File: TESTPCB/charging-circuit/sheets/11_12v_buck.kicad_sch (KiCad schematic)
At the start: 15 parts, among them P8 1.27mm/1*3p, U19 TPS54302DDCR_C311983

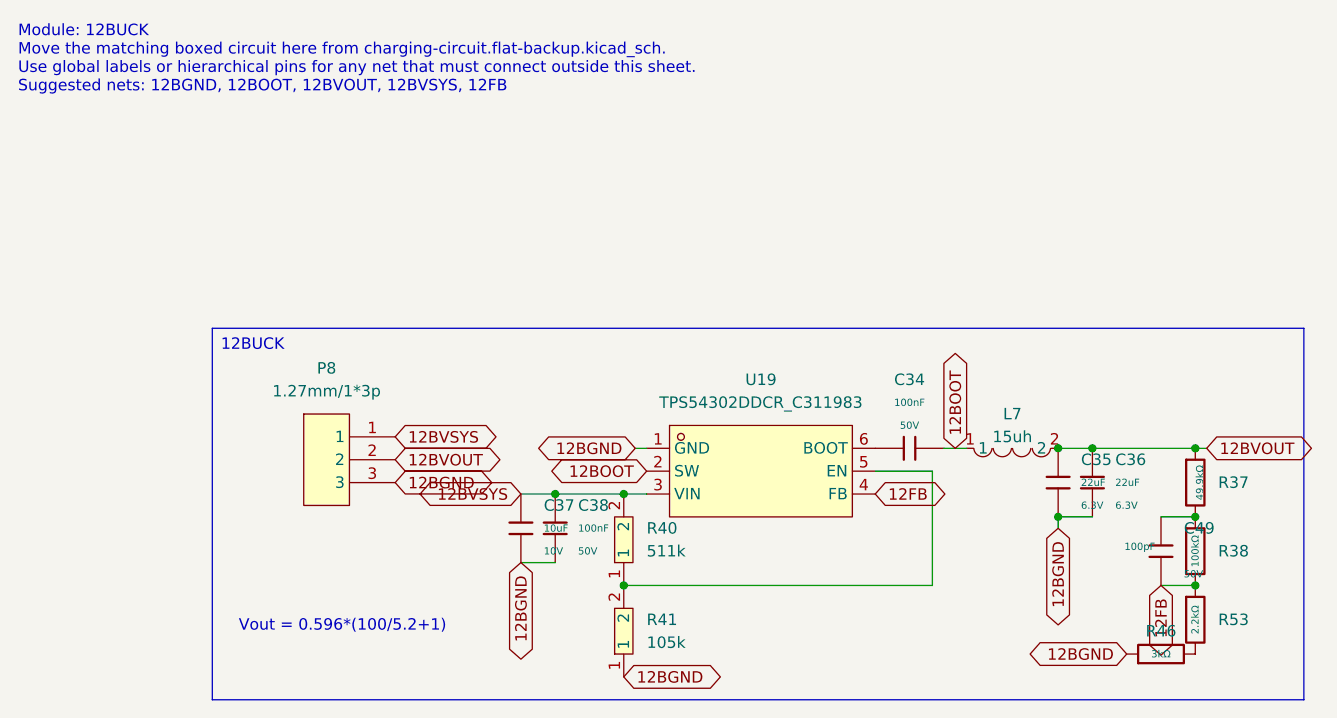
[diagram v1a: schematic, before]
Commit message: Fixed formatting issues, now the hierachal sheets are all labeled as net labels and when we want to expose their pins we will make them into hierchal or global pins
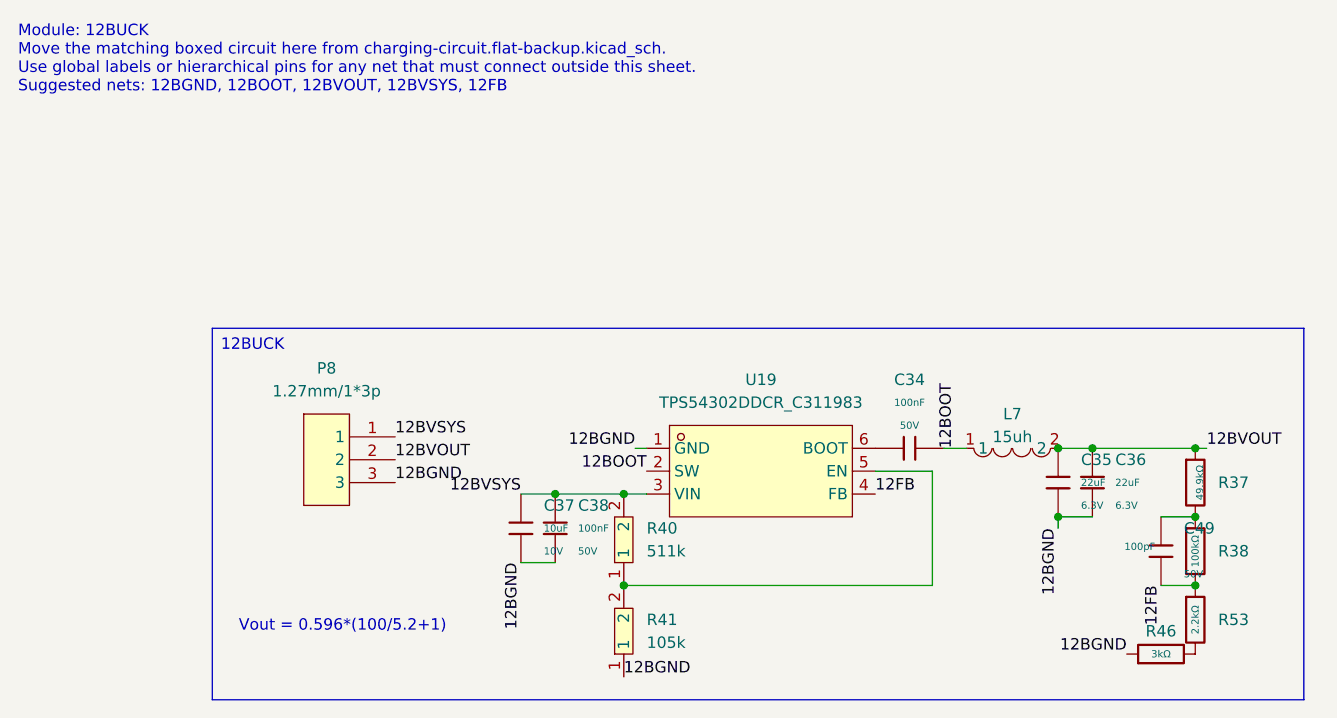
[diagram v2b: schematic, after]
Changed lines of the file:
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@@
 		)
 	)
-	(global_label "12FB"
-		(shape bidirectional)
+	(label "12FB"
 		(at 120.65 73.66 0)
 		(effects
@@
 			(justify left bottom)
 		)
-		(property "Intersheetrefs" "${INTERSHEET_REFS}"
-			(at 120.65 73.66 0)
-			(effects
-				(font
-					(size 1.27 1.27)
-				)
-				(hide yes)
-			)
-		)
 	)
-	(global_label "12BGND"
-		(shape bidirectional)
+	(label "12BGND"
 		(at 140.97 77.47 270)
 		(effects
@@
 			(justify right bottom)
 		)
-		(property "Intersheetrefs" "${INTERSHEET_REFS}"
-			(at 140.97 77.47 0)
-			(effects
-				(font
-					(size 1.27 1.27)
-				)
-				(hide yes)
-			)
-		)
 	)
-	(global_label "12BVOUT"
-		(shape bidirectional)
+	(label "12BVOUT"
 		(at 67.31 69.85 0)
 		(effects
@@
 			(justify left bottom)
 		)
-		(property "Intersheetrefs" "${INTERSHEET_REFS}"
-			(at 67.31 69.85 0)
-			(effects
-				(font
-					(size 1.27 1.27)
-				)
-				(hide yes)
-			)
-		)
 	)
-	(global_label "12BGND"
-		(shape bidirectional)
+	(label "12BGND"
 		(at 67.31 72.39 0)
 		(effects
@@
 			(justify left bottom)
 		)
-		(property "Intersheetrefs" "${INTERSHEET_REFS}"
-			(at 67.31 72.39 0)
-			(effects
-				(font
-					(size 1.27 1.27)
-				)
-				(hide yes)
-			)
-		)
 	)
-	(global_label "12BGND"
-		(shape bidirectional)
+	(label "12BGND"
 		(at 81.28 81.28 270)
 		(effects
@@
 			(justify right bottom)
 		)
-		(property "Intersheetrefs" "${INTERSHEET_REFS}"
-			(at 81.28 81.28 0)
-			(effects
-				(font
-					(size 1.27 1.27)
-				)
-				(hide yes)
-			)
-		)
 	)
-	(global_label "12BGND"
-		(shape bidirectional)
+	(label "12BGND"
 		(at 148.59 91.44 180)
 		(effects
@@
 			(justify right bottom)
 		)
-		(property "Intersheetrefs" "${INTERSHEET_REFS}"
-			(at 148.59 91.44 0)
-			(effects
-				(font
-					(size 1.27 1.27)
-				)
-				(hide yes)
-			)
-		)
 	)
-	(global_label "12BOOT"
-		(shape bidirectional)
+	(label "12BOOT"
 		(at 129.54 68.58 90)
 		(effects
@@
 			(justify left bottom)
 		)
-		(property "Intersheetrefs" "${INTERSHEET_REFS}"
-			(at 129.54 68.58 0)
-			(effects
-				(font
-					(size 1.27 1.27)
-				)
-				(hide yes)
-			)
-		)
 	)
-	(global_label "12BGND"
-		(shape bidirectional)
+	(label "12BGND"
 		(at 93.98 68.58 180)
 		(effects
@@
 			(justify right bottom)
 		)
-		(property "Intersheetrefs" "${INTERSHEET_REFS}"
-			(at 93.98 68.58 0)
-			(effects
-				(font
-					(size 1.27 1.27)
-				)
-				(hide yes)
-			)
-		)
 	)
-	(global_label "12BVOUT"
-		(shape bidirectional)
+	(label "12BVOUT"
 		(at 157.48 68.58 0)
 		(effects
@@
 			(justify left bottom)
 		)
-		(property "Intersheetrefs" "${INTERSHEET_REFS}"
-			(at 157.48 68.58 0)
-			(effects
-				(font
-					(size 1.27 1.27)
-				)
-				(hide yes)
-			)
-		)
 	)
-	(global_label "12FB"
-		(shape bidirectional)
+	(label "12FB"
 		(at 152.4 83.82 270)
 		(effects
@@
 			(justify right bottom)
 		)
-		(property "Intersheetrefs" "${INTERSHEET_REFS}"
-			(at 152.4 83.82 0)
-			(effects
-				(font
-					(size 1.27 1.27)
-				)
-				(hide yes)
-			)
-		)
 	)
-	(global_label "12BVSYS"
-		(shape bidirectional)
+	(label "12BVSYS"
 		(at 67.31 67.31 0)
 		(effects
@@
 			(justify left bottom)
 		)
-		(property "Intersheetrefs" "${INTERSHEET_REFS}"
-			(at 67.31 67.31 0)
-			(effects
-				(font
-					(size 1.27 1.27)
-				)
-				(hide yes)
-			)
-		)
 	)
-	(global_label "12BVSYS"
-		(shape bidirectional)
+	(label "12BVSYS"
 		(at 81.28 73.66 180)
 		(effects
@@
 			(justify right bottom)
 		)
-		(property "Intersheetrefs" "${INTERSHEET_REFS}"
-			(at 81.28 73.66 0)
-			(effects
-				(font
-					(size 1.27 1.27)
-				)
-				(hide yes)
-			)
-		)
 	)
-	(global_label "12BGND"
-		(shape bidirectional)
+	(label "12BGND"
 		(at 92.71 93.98 0)
 		(effects
@@
 			(justify left bottom)
 		)
-		(property "Intersheetrefs" "${INTERSHEET_REFS}"
-			(at 92.71 93.98 0)
-			(effects
-				(font
-					(size 1.27 1.27)
-				)
-				(hide yes)
-			)
-		)
 	)
-	(global_label "12BOOT"
-		(shape bidirectional)
+	(label "12BOOT"
 		(at 95.25 71.12 180)
 		(effects
@@
 			(justify right bottom)
 		)
-		(property "Intersheetrefs" "${INTERSHEET_REFS}"
-			(at 95.25 71.12 0)
-			(effects
-				(font
-					(size 1.27 1.27)
-				)
-				(hide yes)
-			)
-		)
 	)
